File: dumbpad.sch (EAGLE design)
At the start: 39 parts

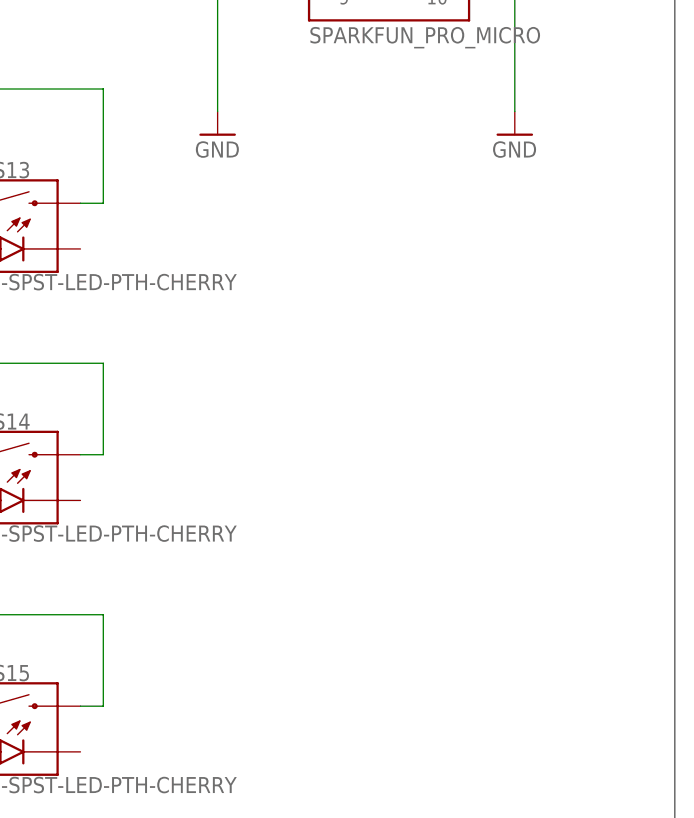
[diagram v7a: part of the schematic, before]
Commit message: added reset button back to v0.5
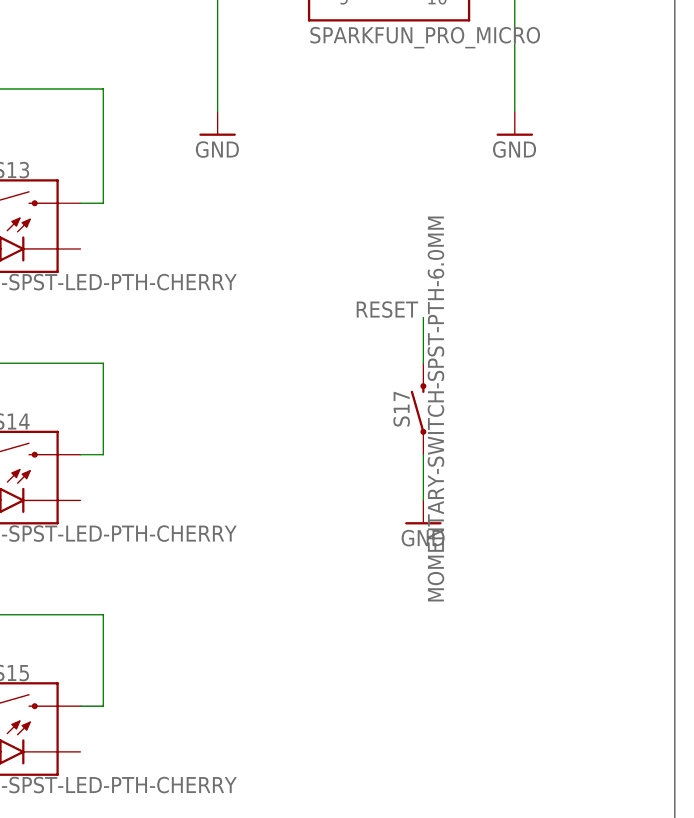
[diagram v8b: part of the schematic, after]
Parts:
- added S17: MOMENTARY-SWITCH-SPST-PTH-6.0MM, SparkFun-Switches:MOMENTARY-SWITCH-SPST-PTH-6.0MM
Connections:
- net GND: now also S17.1
- net RESET: now also S17.2
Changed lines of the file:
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@@
 <part name="R2" library="SparkFun-Resistors" deviceset="330OHM" device="-HORIZ-1/10W-5%" value="330"/>
 <part name="GND2" library="supply1" library_urn="urn:adsk.eagle:library:371" deviceset="GND" device=""/>
+<part name="S17" library="SparkFun-Switches" deviceset="MOMENTARY-SWITCH-SPST" device="-PTH-6.0MM"/>
+<part name="GND4" library="supply1" library_urn="urn:adsk.eagle:library:371" deviceset="GND" device=""/>
 </parts>
 <sheets>
@@
 <attribute name="VALUE" x="162.56" y="124.46" size="1.778" layer="96"/>
 </instance>
+<instance part="S17" gate="G$1" x="287.02" y="78.74" smashed="yes" rot="R90">
+<attribute name="NAME" x="285.496" y="78.74" size="1.778" layer="95" font="vector" rot="R90" align="bottom-center"/>
+<attribute name="VALUE" x="287.528" y="78.74" size="1.778" layer="96" font="vector" rot="R90" align="top-center"/>
+</instance>
+<instance part="GND4" gate="1" x="287.02" y="66.04" smashed="yes">
+<attribute name="VALUE" x="284.48" y="63.5" size="1.778" layer="96"/>
+</instance>
 </instances>
 <busses>
@@
 <pinref part="D19" gate="D1" pin="C"/>
 <wire x1="170.18" y1="132.08" x2="170.18" y2="134.62" width="0.1524" layer="91"/>
+</segment>
+<segment>
+<pinref part="S17" gate="G$1" pin="1"/>
+<wire x1="287.02" y1="73.66" x2="287.02" y2="68.58" width="0.1524" layer="91"/>
+<pinref part="GND4" gate="1" pin="GND"/>
 </segment>
 </net>
@@
 <label x="304.8" y="147.32" size="1.778" layer="95"/>
 </segment>
-</net>
+<segment>
+<pinref part="S17" gate="G$1" pin="2"/>
+<wire x1="287.02" y1="83.82" x2="287.02" y2="88.9" width="0.1524" layer="91"/>
+<label x="279.4" y="88.9" size="1.778" layer="95"/>
+</segment>
+</net>
